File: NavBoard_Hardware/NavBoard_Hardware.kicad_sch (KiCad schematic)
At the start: 0 parts

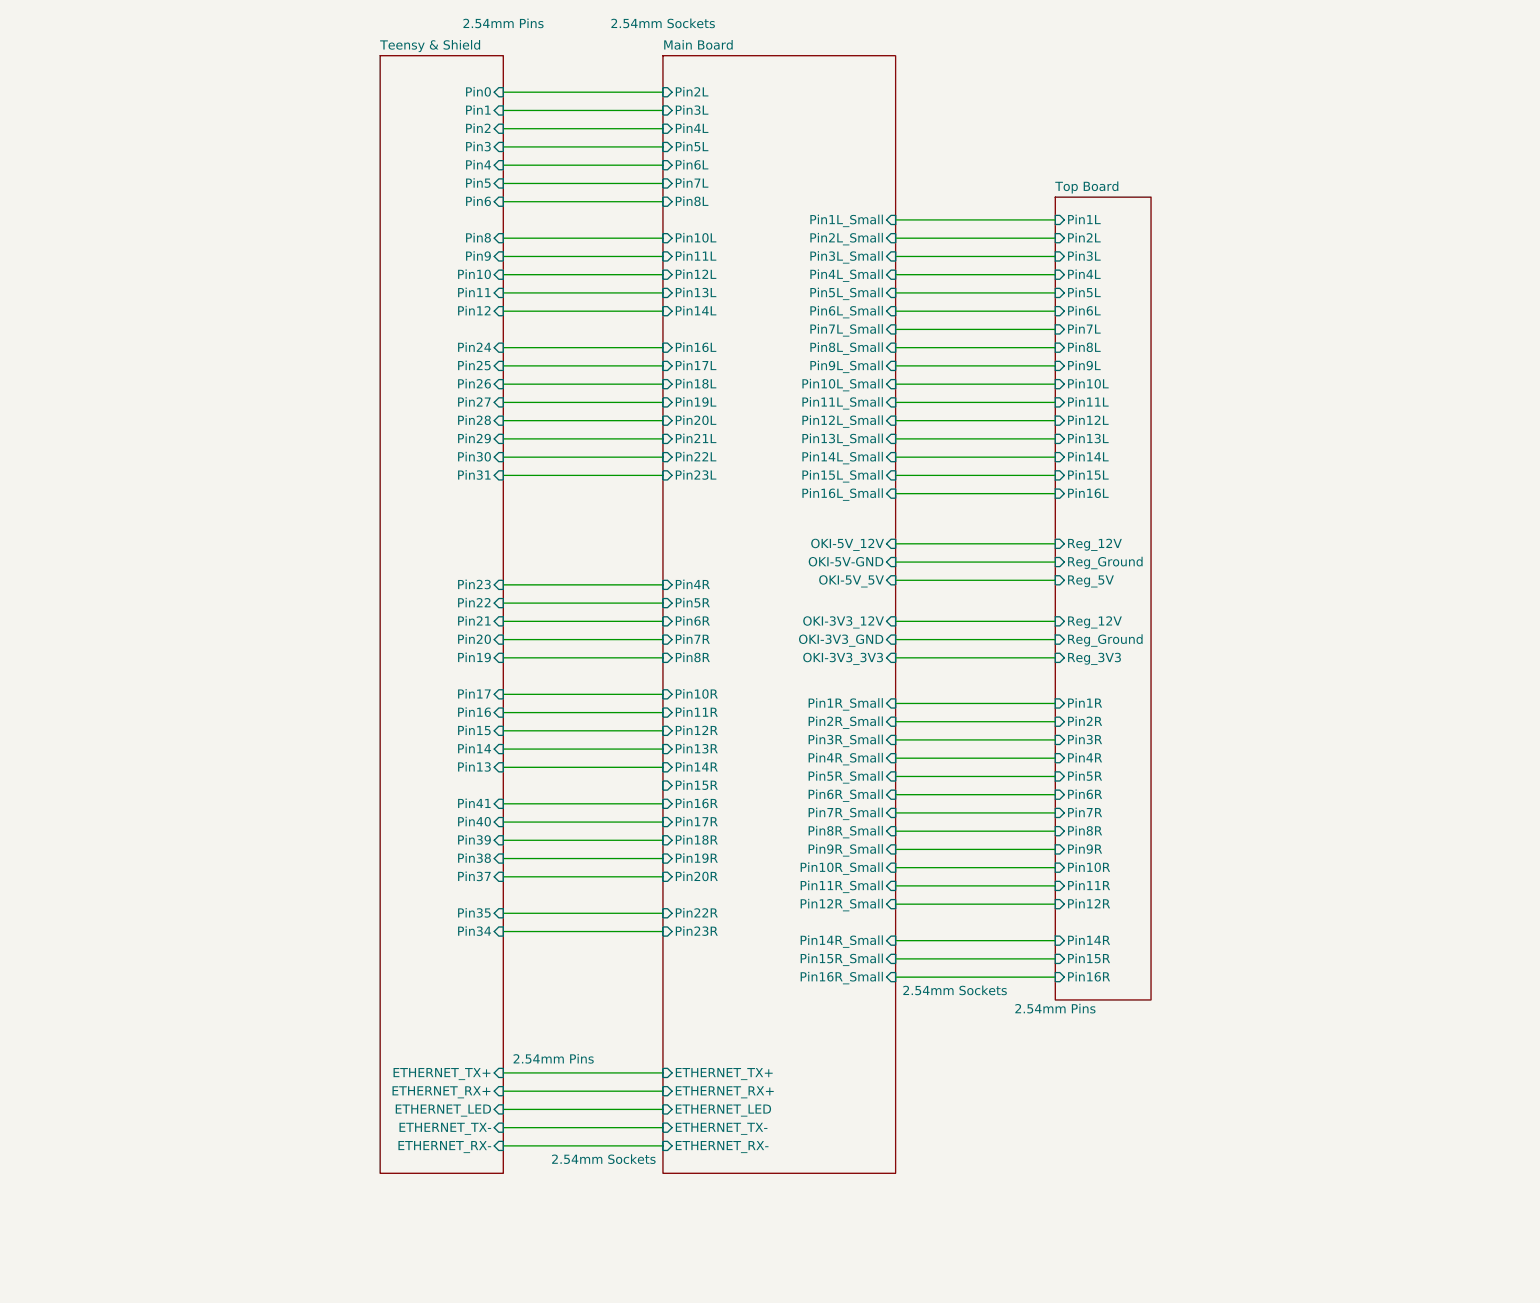
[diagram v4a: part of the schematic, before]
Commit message: Rearranged schematic
I realize now that this is a dumb idea...
Going to redesign the board so the teensy just sits on top
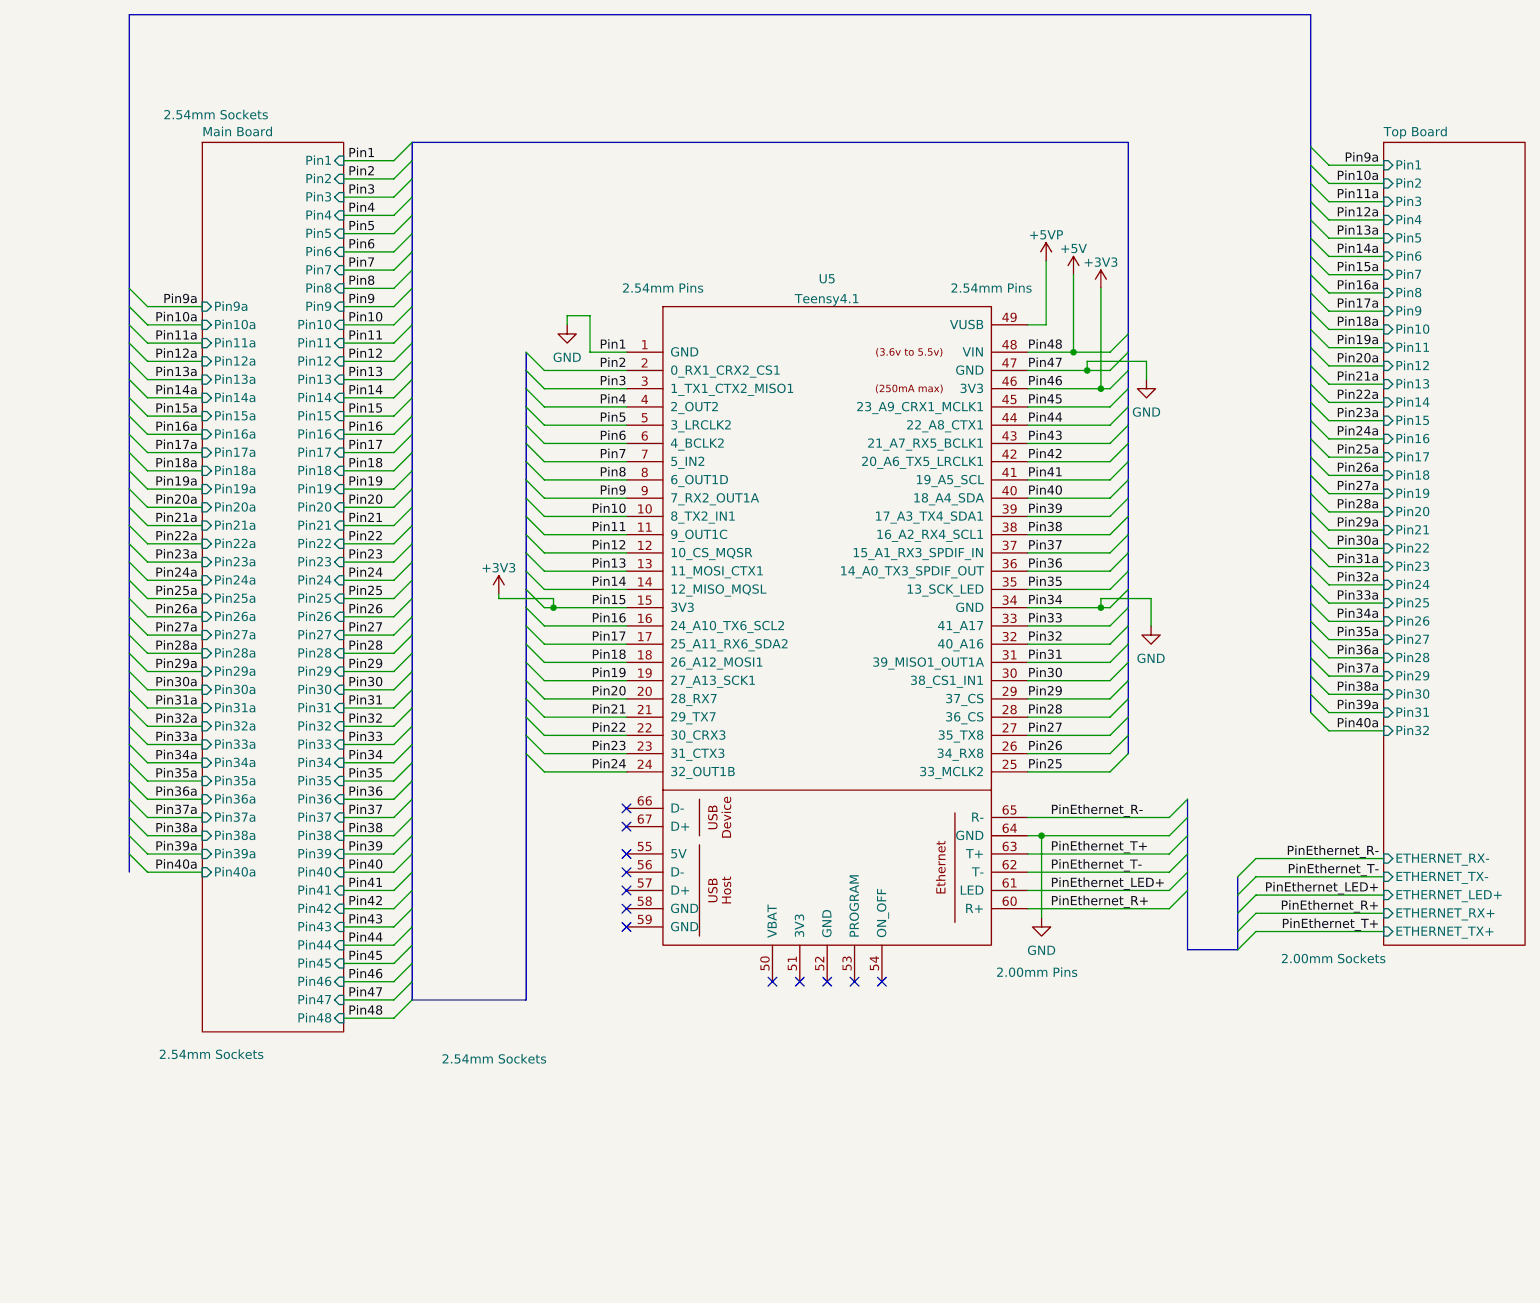
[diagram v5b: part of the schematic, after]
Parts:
- added U5: Teensy4.1, teensy:Teensy41, symbol teensy:Teensy4.1
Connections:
- new net +3V3: U5.15 (3V3), U5.46 (3V3)
- new net +5V: U5.48 (VIN)
- new net +5VP: U5.49 (VUSB)
- new net GND: U5.1 (GND), U5.34 (GND), U5.47 (GND), U5.64 (GND)
- new net Pin10: U5.10 (8_TX2_IN1)
- new net Pin11: U5.11 (9_OUT1C)
- new net Pin12: U5.12 (10_CS_MQSR)
- new net Pin13: U5.13 (11_MOSI_CTX1)
- new net Pin14: U5.14 (12_MISO_MQSL)
- new net Pin16: U5.16 (24_A10_TX6_SCL2)
- new net Pin17: U5.17 (25_A11_RX6_SDA2)
- new net Pin18: U5.18 (26_A12_MOSI1)
- new net Pin19: U5.19 (27_A13_SCK1)
- new net Pin2: U5.2 (0_RX1_CRX2_CS1)
- new net Pin20: U5.20 (28_RX7)
- new net Pin21: U5.21 (29_TX7)
- new net Pin22: U5.22 (30_CRX3)
- new net Pin23: U5.23 (31_CTX3)
- new net Pin24: U5.24 (32_OUT1B)
- new net Pin25: U5.25 (33_MCLK2)
- new net Pin26: U5.26 (34_RX8)
- new net Pin27: U5.27 (35_TX8)
- new net Pin28: U5.28 (36_CS)
- new net Pin29: U5.29 (37_CS)
- new net Pin3: U5.3 (1_TX1_CTX2_MISO1)
- new net Pin30: U5.30 (38_CS1_IN1)
- new net Pin31: U5.31 (39_MISO1_OUT1A)
- new net Pin32: U5.32 (40_A16)
- new net Pin33: U5.33 (41_A17)
- new net Pin35: U5.35 (13_SCK_LED)
- new net Pin36: U5.36 (14_A0_TX3_SPDIF_OUT)
- new net Pin37: U5.37 (15_A1_RX3_SPDIF_IN)
- new net Pin38: U5.38 (16_A2_RX4_SCL1)
- new net Pin39: U5.39 (17_A3_TX4_SDA1)
- new net Pin4: U5.4 (2_OUT2)
- new net Pin40: U5.40 (18_A4_SDA)
- new net Pin41: U5.41 (19_A5_SCL)
- new net Pin42: U5.42 (20_A6_TX5_LRCLK1)
- new net Pin43: U5.43 (21_A7_RX5_BCLK1)
- new net Pin44: U5.44 (22_A8_CTX1)
- new net Pin45: U5.45 (23_A9_CRX1_MCLK1)
- new net Pin5: U5.5 (3_LRCLK2)
- new net Pin6: U5.6 (4_BCLK2)
- new net Pin7: U5.7 (5_IN2)
- new net Pin8: U5.8 (6_OUT1D)
- new net Pin9: U5.9 (7_RX2_OUT1A)
- new net PinEthernet_LED+: U5.61 (LED)
- new net PinEthernet_R+: U5.60 (R+)
- new net PinEthernet_R-: U5.65 (R-)
- new net PinEthernet_T+: U5.63 (T+)
- new net PinEthernet_T-: U5.62 (T-)
- no-connect marks 0 -> 12
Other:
- removed sheet Teensy & Shield
- sheet Main Board ports: added Pin1, Pin10, Pin10a, Pin11, Pin11a, Pin12, Pin12a, Pin13, Pin13a, Pin14, Pin14a, Pin15, Pin15a, Pin16, Pin16a, Pin17, Pin17a, Pin18, Pin18a, Pin19, Pin19a, Pin2, Pin20, Pin20a, Pin21, Pin21a, Pin22, Pin22a, Pin23, Pin23a, Pin24, Pin24a, Pin25, Pin25a, Pin26, Pin26a, Pin27, Pin27a, Pin28, Pin28a, Pin29, Pin29a, Pin3, Pin30, Pin30a, Pin31, Pin31a, Pin32, Pin32a, Pin33, Pin33a, Pin34, Pin34a, Pin35, Pin35a, Pin36, Pin36a, Pin37, Pin37a, Pin38, Pin38a, Pin39, Pin39a, Pin4, Pin40, Pin40a, Pin41, Pin42, Pin43, Pin44, Pin45, Pin46, Pin47, Pin48, Pin5, Pin6, Pin7, Pin8, Pin9, Pin9a; removed ETHERNET_LED, ETHERNET_RX+, ETHERNET_RX-, ETHERNET_TX+, ETHERNET_TX-, OKI-3V3_12V, OKI-3V3_3V3, OKI-3V3_GND, OKI-5V-GND, OKI-5V_12V, OKI-5V_5V, Pin10L, Pin10L_Small, Pin10R, Pin10R_Small, Pin11L, Pin11L_Small, Pin11R, Pin11R_Small, Pin12L, Pin12L_Small, Pin12R, Pin12R_Small, Pin13L, Pin13L_Small, Pin13R, Pin14L, Pin14L_Small, Pin14R, Pin14R_Small, Pin15L_Small, Pin15R, Pin15R_Small, Pin16L, Pin16L_Small, Pin16R, Pin16R_Small, Pin17L, Pin17R, Pin18L, Pin18R, Pin19L, Pin19R, Pin1L_Small, Pin1R_Small, Pin20L, Pin20R, Pin21L, Pin22L, Pin22R, Pin23L, Pin23R, Pin2L, Pin2L_Small, Pin2R_Small, Pin3L, Pin3L_Small, Pin3R_Small, Pin4L, Pin4L_Small, Pin4R, Pin4R_Small, Pin5L, Pin5L_Small, Pin5R, Pin5R_Small, Pin6L, Pin6L_Small, Pin6R, Pin6R_Small, Pin7L, Pin7L_Small, Pin7R, Pin7R_Small, Pin8L, Pin8L_Small, Pin8R, Pin8R_Small, Pin9L_Small, Pin9R_Small
- sheet Top Board ports: added ETHERNET_LED+, ETHERNET_RX+, ETHERNET_RX-, ETHERNET_TX+, ETHERNET_TX-, Pin1, Pin10, Pin11, Pin12, Pin13, Pin14, Pin15, Pin16, Pin17, Pin18, Pin19, Pin2, Pin20, Pin21, Pin22, Pin23, Pin24, Pin25, Pin26, Pin27, Pin28, Pin29, Pin3, Pin30, Pin31, Pin32, Pin4, Pin5, Pin6, Pin7, Pin8, Pin9; removed Pin10L, Pin10R, Pin11L, Pin11R, Pin12L, Pin12R, Pin13L, Pin14L, Pin14R, Pin15L, Pin15R, Pin16L, Pin16R, Pin1L, Pin1R, Pin2L, Pin2R, Pin3L, Pin3R, Pin4L, Pin4R, Pin5L, Pin5R, Pin6L, Pin6R, Pin7L, Pin7R, Pin8L, Pin8R, Pin9L, Pin9R, Reg_12V, Reg_3V3, Reg_5V, Reg_Ground

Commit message: Decided on pcb layout
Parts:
- U5: footprint teensy:Teensy41 -> Nav_Board:Teensy41_Suspended
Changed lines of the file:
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@@
   (symbol (lib_id "power:+5V") (at 175.26 56.515 0) (unit 1)
     (in_bom yes) (on_board yes) (fields_autoplaced)
-    (property "Reference" "#PWR?" (id 0) (at 175.26 60.325 0)
+    (property "Reference" "#PWR0120" (id 0) (at 175.26 60.325 0)
       (effects (font (size 1.27 1.27)) hide)
     )
@@
   (symbol (lib_id "power:+5VP") (at 171.45 54.61 0) (unit 1)
     (in_bom yes) (on_board yes) (fields_autoplaced)
-    (property "Reference" "#PWR?" (id 0) (at 171.45 58.42 0)
+    (property "Reference" "#PWR0117" (id 0) (at 171.45 58.42 0)
       (effects (font (size 1.27 1.27)) hide)
     )
@@
   (symbol (lib_id "power:+3V3") (at 179.07 58.42 0) (unit 1)
     (in_bom yes) (on_board yes) (fields_autoplaced)
-    (property "Reference" "#PWR?" (id 0) (at 179.07 62.23 0)
+    (property "Reference" "#PWR0119" (id 0) (at 179.07 62.23 0)
       (effects (font (size 1.27 1.27)) hide)
     )
@@
   (symbol (lib_id "power:GND") (at 104.775 63.5 0) (unit 1)
     (in_bom yes) (on_board yes) (fields_autoplaced)
-    (property "Reference" "#PWR?" (id 0) (at 104.775 69.85 0)
+    (property "Reference" "#PWR0106" (id 0) (at 104.775 69.85 0)
       (effects (font (size 1.27 1.27)) hide)
     )
@@
   (symbol (lib_id "power:+3V3") (at 95.25 100.965 0) (unit 1)
     (in_bom yes) (on_board yes) (fields_autoplaced)
-    (property "Reference" "#PWR?" (id 0) (at 95.25 104.775 0)
+    (property "Reference" "#PWR0105" (id 0) (at 95.25 104.775 0)
       (effects (font (size 1.27 1.27)) hide)
     )
@@
   (symbol (lib_id "power:GND") (at 185.42 71.12 0) (unit 1)
     (in_bom yes) (on_board yes) (fields_autoplaced)
-    (property "Reference" "#PWR?" (id 0) (at 185.42 77.47 0)
+    (property "Reference" "#PWR0114" (id 0) (at 185.42 77.47 0)
       (effects (font (size 1.27 1.27)) hide)
     )
@@
   (symbol (lib_id "power:GND") (at 170.815 146.05 0) (unit 1)
     (in_bom yes) (on_board yes) (fields_autoplaced)
-    (property "Reference" "#PWR?" (id 0) (at 170.815 152.4 0)
+    (property "Reference" "#PWR0118" (id 0) (at 170.815 152.4 0)
       (effects (font (size 1.27 1.27)) hide)
     )
@@
   (symbol (lib_id "power:GND") (at 186.055 105.41 0) (unit 1)
     (in_bom yes) (on_board yes) (fields_autoplaced)
-    (property "Reference" "#PWR?" (id 0) (at 186.055 111.76 0)
+    (property "Reference" "#PWR0113" (id 0) (at 186.055 111.76 0)
       (effects (font (size 1.27 1.27)) hide)
     )
@@
     (property "Reference" "U5" (id 0) (at 140.97 57.1205 0))
     (property "Value" "Teensy4.1" (id 1) (at 140.97 59.8956 0))
-    (property "Footprint" "teensy:Teensy41" (id 2) (at 130.81 111.76 0)
+    (property "Footprint" "Nav_Board:Teensy41_Suspended" (id 2) (at 130.81 111.76 0)
       (effects (font (size 1.27 1.27)) hide)
     )
@@
       (reference "#PWR0104") (unit 1) (value "GND") (footprint "")
     )
+    (path "/8cbfafcb-fb7f-4766-b177-29172074bff6"
+      (reference "#PWR0105") (unit 1) (value "+3V3") (footprint "")
+    )
+    (path "/7281335f-b70f-437c-818b-9f20564b0909"
+      (reference "#PWR0106") (unit 1) (value "GND") (footprint "")
+    )
     (path "/1cf30331-e31a-4dae-8418-1a281b51585f/95aece0b-b52d-44f9-8cec-c562feeb9a81"
       (reference "#PWR0107") (unit 1) (value "GND") (footprint "")
@@
       (reference "#PWR0112") (unit 1) (value "GND") (footprint "")
     )
+    (path "/e4cf636c-1576-4f89-8838-acb00e43ed9f"
+      (reference "#PWR0113") (unit 1) (value "GND") (footprint "")
+    )
+    (path "/b214e2d5-ee1c-420a-aa97-9862ca362859"
+      (reference "#PWR0114") (unit 1) (value "GND") (footprint "")
+    )
     (path "/1cf30331-e31a-4dae-8418-1a281b51585f/56a938ea-1593-4fd2-8ea5-ab347d02104e"
       (reference "#PWR0115") (unit 1) (value "GND") (footprint "")
@@
       (reference "#PWR0116") (unit 1) (value "GND") (footprint "")
     )
+    (path "/60a05e60-9e13-45f1-a805-f4f4f0f27f20"
+      (reference "#PWR0117") (unit 1) (value "+5VP") (footprint "")
+    )
+    (path "/d2c60703-915d-49d4-8601-d1929e6cc3ae"
+      (reference "#PWR0118") (unit 1) (value "GND") (footprint "")
+    )
+    (path "/67c33bc3-7989-42db-8a66-e00738287920"
+      (reference "#PWR0119") (unit 1) (value "+3V3") (footprint "")
+    )
+    (path "/32a33af1-8dcb-42a1-94be-0f66cb9e1241"
+      (reference "#PWR0120") (unit 1) (value "+5V") (footprint "")
+    )
+    (path "/1cf30331-e31a-4dae-8418-1a281b51585f/0e0c640d-a895-4212-a4dc-6549d969ffca/eb60033f-c0ce-494b-ac86-61fcfdb86753"
+      (reference "#PWR0121") (unit 1) (value "GND") (footprint "")
+    )
+    (path "/1cf30331-e31a-4dae-8418-1a281b51585f/0e0c640d-a895-4212-a4dc-6549d969ffca/d68453b9-4a43-4dae-bbf5-117fb086d81c"
+      (reference "#PWR0122") (unit 1) (value "+12V") (footprint "")
+    )
+    (path "/1cf30331-e31a-4dae-8418-1a281b51585f/0e0c640d-a895-4212-a4dc-6549d969ffca/addb7395-a76d-40ba-8d1b-8fc9d951db77"
+      (reference "#PWR0123") (unit 1) (value "+5V") (footprint "")
+    )
+    (path "/1cf30331-e31a-4dae-8418-1a281b51585f/9d5aae42-0135-4753-bd18-74377e77564d"
+      (reference "#PWR0124") (unit 1) (value "GND") (footprint "")
+    )
+    (path "/1cf30331-e31a-4dae-8418-1a281b51585f/cc96963e-15cd-4840-94d4-6431d017121d"
+      (reference "#PWR0125") (unit 1) (value "GND") (footprint "")
+    )
     (path "/1cf30331-e31a-4dae-8418-1a281b51585f/20eae500-0d53-4f5d-9fb8-2022a6fbded9"
-      (reference "#PWR?") (unit 1) (value "GND") (footprint "")
-    )
-    (path "/32a33af1-8dcb-42a1-94be-0f66cb9e1241"
-      (reference "#PWR?") (unit 1) (value "+5V") (footprint "")
-    )
-    (path "/60a05e60-9e13-45f1-a805-f4f4f0f27f20"
-      (reference "#PWR?") (unit 1) (value "+5VP") (footprint "")
-    )
-    (path "/67c33bc3-7989-42db-8a66-e00738287920"
-      (reference "#PWR?") (unit 1) (value "+3V3") (footprint "")
-    )
-    (path "/7281335f-b70f-437c-818b-9f20564b0909"
-      (reference "#PWR?") (unit 1) (value "GND") (footprint "")
+      (reference "#PWR0126") (unit 1) (value "GND") (footprint "")
     )
     (path "/1cf30331-e31a-4dae-8418-1a281b51585f/8ae7e12f-18d6-4957-bfa3-ff1ba42c8ea1"
-      (reference "#PWR?") (unit 1) (value "GND") (footprint "")
-    )
-    (path "/8cbfafcb-fb7f-4766-b177-29172074bff6"
-      (reference "#PWR?") (unit 1) (value "+3V3") (footprint "")
-    )
-    (path "/1cf30331-e31a-4dae-8418-1a281b51585f/9d5aae42-0135-4753-bd18-74377e77564d"
-      (reference "#PWR?") (unit 1) (value "GND") (footprint "")
+      (reference "#PWR0127") (unit 1) (value "GND") (footprint "")
+    )
+    (path "/1cf30331-e31a-4dae-8418-1a281b51585f/d802389d-edcb-4820-b385-71ea841633d1"
+      (reference "#PWR0128") (unit 1) (value "GND") (footprint "")
     )
     (path "/1cf30331-e31a-4dae-8418-1a281b51585f/9dabd508-82e7-453f-bda5-e2986df8dbb5"
-      (reference "#PWR?") (unit 1) (value "+12V") (footprint "")
-    )
-    (path "/1cf30331-e31a-4dae-8418-1a281b51585f/0e0c640d-a895-4212-a4dc-6549d969ffca/addb7395-a76d-40ba-8d1b-8fc9d951db77"
-      (reference "#PWR?") (unit 1) (value "+5V") (footprint "")
-    )
-    (path "/b214e2d5-ee1c-420a-aa97-9862ca362859"
-      (reference "#PWR?") (unit 1) (value "GND") (footprint "")
+      (reference "#PWR0129") (unit 1) (value "+12V") (footprint "")
     )
     (path "/1cf30331-e31a-4dae-8418-1a281b51585f/c52ac31b-05e6-4573-bf16-5d77c9e5314f"
-      (reference "#PWR?") (unit 1) (value "+5V") (footprint "")
-    )
-    (path "/1cf30331-e31a-4dae-8418-1a281b51585f/cc96963e-15cd-4840-94d4-6431d017121d"
-      (reference "#PWR?") (unit 1) (value "GND") (footprint "")
-    )
-    (path "/d2c60703-915d-49d4-8601-d1929e6cc3ae"
-      (reference "#PWR?") (unit 1) (value "GND") (footprint "")
+      (reference "#PWR0130") (unit 1) (value "+5V") (footprint "")
     )
     (path "/1cf30331-e31a-4dae-8418-1a281b51585f/d4518b53-9b28-4a9e-9187-48c5875212c9"
-      (reference "#PWR?") (unit 1) (value "GND") (footprint "")
-    )
-    (path "/1cf30331-e31a-4dae-8418-1a281b51585f/0e0c640d-a895-4212-a4dc-6549d969ffca/d68453b9-4a43-4dae-bbf5-117fb086d81c"
-      (reference "#PWR?") (unit 1) (value "+12V") (footprint "")
-    )
-    (path "/1cf30331-e31a-4dae-8418-1a281b51585f/d802389d-edcb-4820-b385-71ea841633d1"
-      (reference "#PWR?") (unit 1) (value "GND") (footprint "")
-    )
-    (path "/e4cf636c-1576-4f89-8838-acb00e43ed9f"
-      (reference "#PWR?") (unit 1) (value "GND") (footprint "")
-    )
-    (path "/1cf30331-e31a-4dae-8418-1a281b51585f/0e0c640d-a895-4212-a4dc-6549d969ffca/eb60033f-c0ce-494b-ac86-61fcfdb86753"
-      (reference "#PWR?") (unit 1) (value "GND") (footprint "")
+      (reference "#PWR0131") (unit 1) (value "GND") (footprint "")
     )
     (path "/1cf30331-e31a-4dae-8418-1a281b51585f/cfa695dc-e859-4ad7-a02d-ada1f7512f16/d997983e-985b-4240-8c4e-c57a43eedad7"
@@
     )
     (path "/f85acb57-ceaf-4701-afed-262e01bc5f08"
-      (reference "U5") (unit 1) (value "Teensy4.1") (footprint "teensy:Teensy41")
+      (reference "U5") (unit 1) (value "Teensy4.1") (footprint "Nav_Board:Teensy41_Suspended")
     )
     (path "/1cf30331-e31a-4dae-8418-1a281b51585f/0e0c640d-a895-4212-a4dc-6549d969ffca/e8067ed1-f723-45e3-86a9-60164243f6b4"
-      (reference "U?") (unit 1) (value "OKI-5V") (footprint "MRDT_Devices:OKI_Horizontal")
-    )
-  )
+      (reference "U?") (unit 1) (value "OKI-5V") (footprint "Converter_DCDC:Converter_DCDC_Murata_OKI-78SR_Vertical")
+    )
+  )
